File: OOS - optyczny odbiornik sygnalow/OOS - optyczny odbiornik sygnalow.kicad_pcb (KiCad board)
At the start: 2 copper layers, 31 x 47 mm, 52 parts, among them J1 Conn_01x02_Socket, J2 Conn_01x02_Socket, J3 Conn_01x02_Socket, J4 Conn_01x02_Socket, J5 Conn_Coaxial, U1 OPA300AIDBVR, U2 OPA300AIDBVR

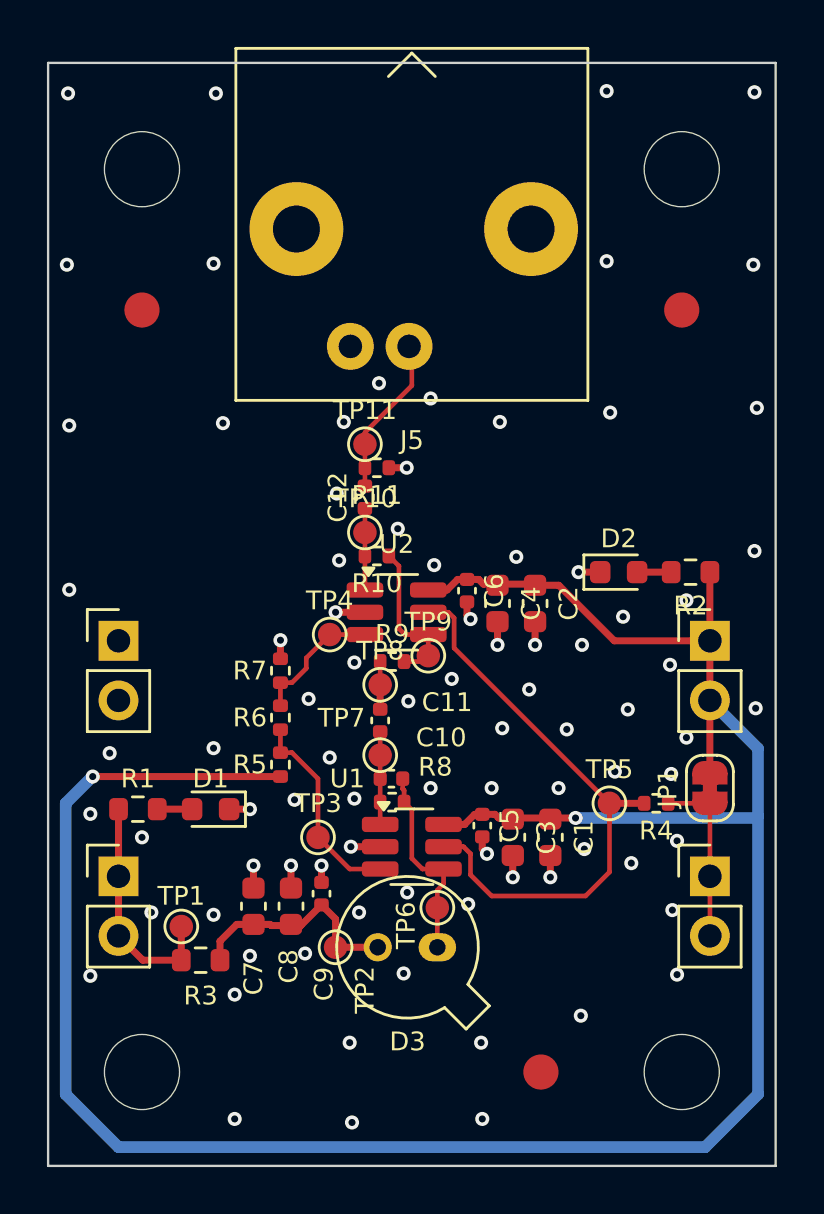
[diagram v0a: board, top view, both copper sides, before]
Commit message: Wyczyszczenie schematu i PCB (Ustalenie wymiarowania, Charakterystyki PCB)
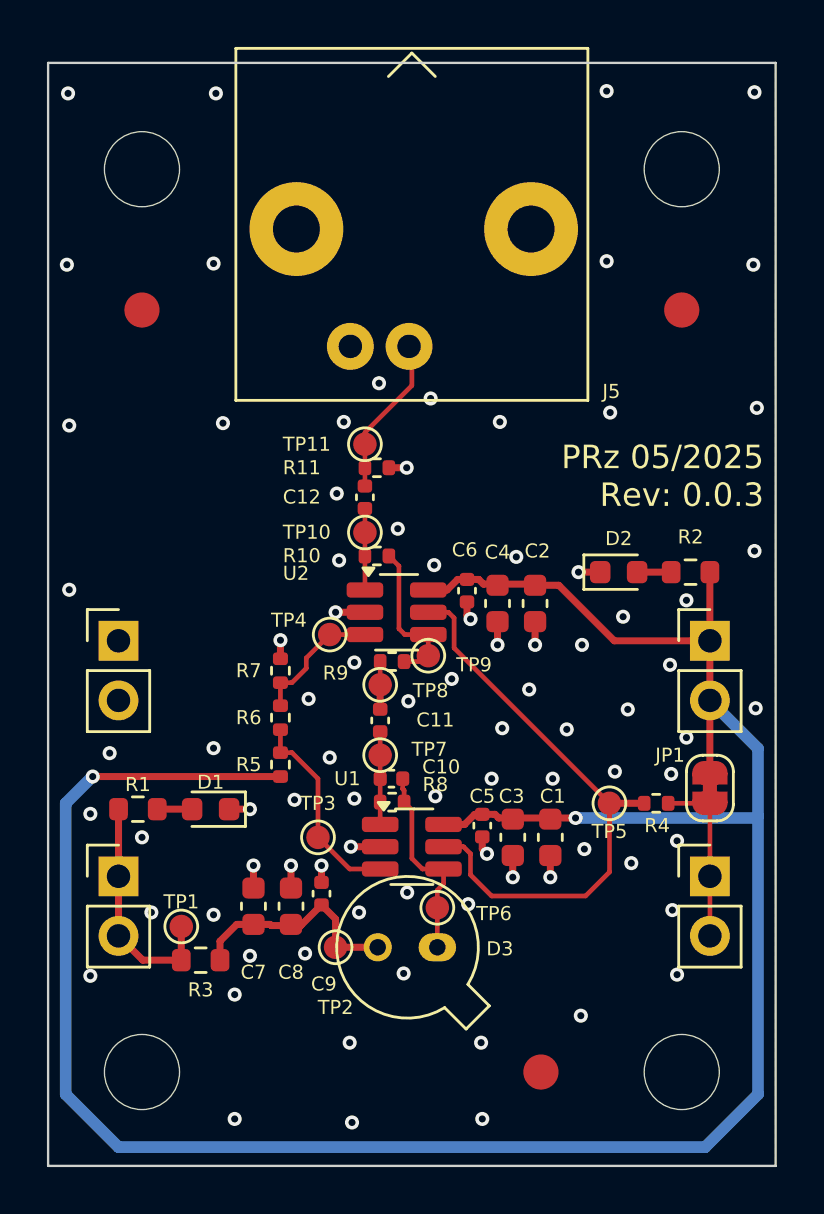
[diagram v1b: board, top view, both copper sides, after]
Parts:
- added REF**: ESD-Logo_6.6x6mm_SilkScreen, Symbol:ESD-Logo_6.6x6mm_SilkScreen, B.Cu at (192.9, 99.4)
- added REF**: WEEE-Logo_4.2x6mm_SilkScreen, Symbol:WEEE-Logo_4.2x6mm_SilkScreen, B.Cu at (184.9, 99.8)
- added REF**: KiCad-Logo2_5mm_SilkScreen, Symbol:KiCad-Logo2_5mm_SilkScreen, B.Cu at (188.4, 91.4)
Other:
- board text added: "0"
- board text added: "0 mm"
- board text added: "0,01 mm"
- board text added: "0,02"
- board text added: "0,035 mm"
- board text added: "0,1600 mm / 0,1000 mm"
- board text added: "0,2500 mm"
- board text added: "1"
- board text added: "1,51 mm"
- board text added: "1,6000 mm"
- board text added: "2"
- board text added: "3,3"
- board text added: "31,0000 mm x 47,0000 mm"
- board text added: "4,5"
- board text added: "B.Cu"
- board text added: "B.Mask"
- board text added: "B.Silkscreen"
- board text added: "Bottom Silk Screen"
- board text added: "Bottom Solder Mask"
- board text added: "CHARAKTERYSTYKA PŁYTKI"
- board text added: "Całkowity rozmiar płytki:"
- board text added: "Dielektryk"
- board text added: "Epsilon R"
- board text added: "F.Cu"
- board text added: "F.Mask"
- board text added: "F.Silkscreen"
- board text added: "FR4"
- board text added: "FR4 natural"
- board text added: "Green"
- board text added: "Grubość (w mm)"
- board text added: "Grubość płytki:"
- board text added: "HAL lead-free"
- board text added: "Kolor"
- board text added: "Kontrola impedancji:"
- board text added: "Liczba warstw sygnałowych:"
- board text added: "Liquid Ink"
- board text added: "Liquid Photo"
- board text added: "Materiał"
- board text added: "Minimalna ścieżka/odstęp:"
- board text added: "Minimalna średnica otworu:"
- board text added: "Nazwa warstwy"
- board text added: "Nie"
- board text added: "PRz 05/2025 Rev: 0.0.3"
- board text added: "Pokrycie brzegu płytki:"
- board text added: "Pola z kastelacją:"
- board text added: "Tangens strat"
- board text added: "Top Silk Screen"
- board text added: "Top Solder Mask"
- board text added: "Typ"
- board text added: "White"
- board text added: "Wykończenie miedzi:"
- board text added: "Złącza krawędziowe:"
- board text added: "copper"
- board text added: "core"
